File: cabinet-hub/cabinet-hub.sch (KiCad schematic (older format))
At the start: 10 parts, among them P1 Controller, P10 Led4, P2 Sensor1, P3 Sensor2, P4 Sensor3, P5 Sensor4, P6 Sensor5, P7 Led1, P8 Led2, P9 Led3

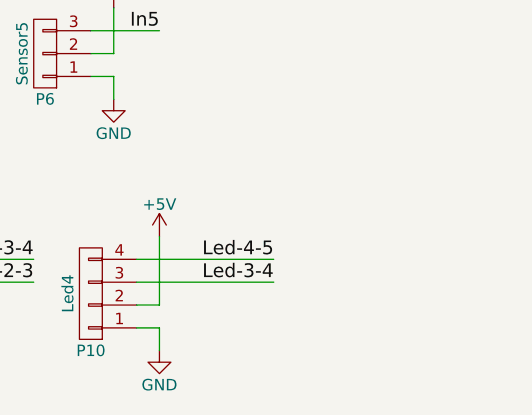
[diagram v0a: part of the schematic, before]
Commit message: Add more LED port
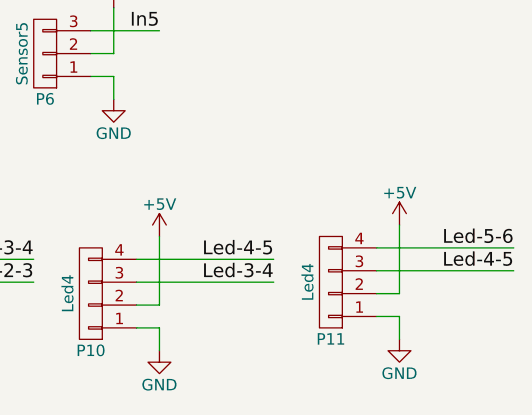
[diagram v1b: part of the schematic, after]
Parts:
- added P11: Led4, Connectors_JST:JST_PH_B4B-PH-K_04x2.00mm_Straight, symbol CONN_01X04
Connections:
- net +5V: now also P11.2 (P2)
- net GND: now also P11.1 (P1)
- net Led-4-5: now also P11.3 (P3)
- new net Led-5-6: P11.4 (P4)
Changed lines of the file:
@@
 Wire Wire Line
 	5450 2100 6050 2100
+$Comp
+L CONN_01X04 P11
+U 1 1 57E76556
+P 6300 2200
+F 0 "P11" H 6300 2450 50  0000 C CNN
+F 1 "Led4" V 6400 2200 50  0000 C CNN
+F 2 "Connectors_JST:JST_PH_B4B-PH-K_04x2.00mm_Straight" H 6300 2200 50  0001 C CNN
+F 3 "" H 6300 2200 50  0000 C CNN
+	1    6300 2200
+	-1   0    0    1
+$EndComp
+$Comp
+L GND #PWR021
+U 1 1 57E7655C
+P 6600 2450
+F 0 "#PWR021" H 6600 2200 50  0001 C CNN
+F 1 "GND" H 6600 2300 50  0000 C CNN
+F 2 "" H 6600 2450 50  0000 C CNN
+F 3 "" H 6600 2450 50  0000 C CNN
+	1    6600 2450
+	1    0    0    -1
+$EndComp
+$Comp
+L +5V #PWR022
+U 1 1 57E76562
+P 6600 1950
+F 0 "#PWR022" H 6600 1800 50  0001 C CNN
+F 1 "+5V" H 6600 2090 50  0000 C CNN
+F 2 "" H 6600 1950 50  0000 C CNN
+F 3 "" H 6600 1950 50  0000 C CNN
+	1    6600 1950
+	1    0    0    -1
+$EndComp
+Wire Wire Line
+	6500 2250 6600 2250
+Wire Wire Line
+	6600 2250 6600 1950
+Wire Wire Line
+	6500 2350 6600 2350
+Wire Wire Line
+	6600 2350 6600 2450
+Text Label 7100 2150 2    60   ~ 0
+Led-4-5
+Wire Wire Line
+	6500 2150 7100 2150
+Text Label 7100 2050 2    60   ~ 0
+Led-5-6
+Wire Wire Line
+	6500 2050 7100 2050
 $EndSCHEMATC
